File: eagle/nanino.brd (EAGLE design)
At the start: 68.6 x 53.3 mm, 19 parts, among them IC1 ATMEGA328P-20, Q1 16MHz

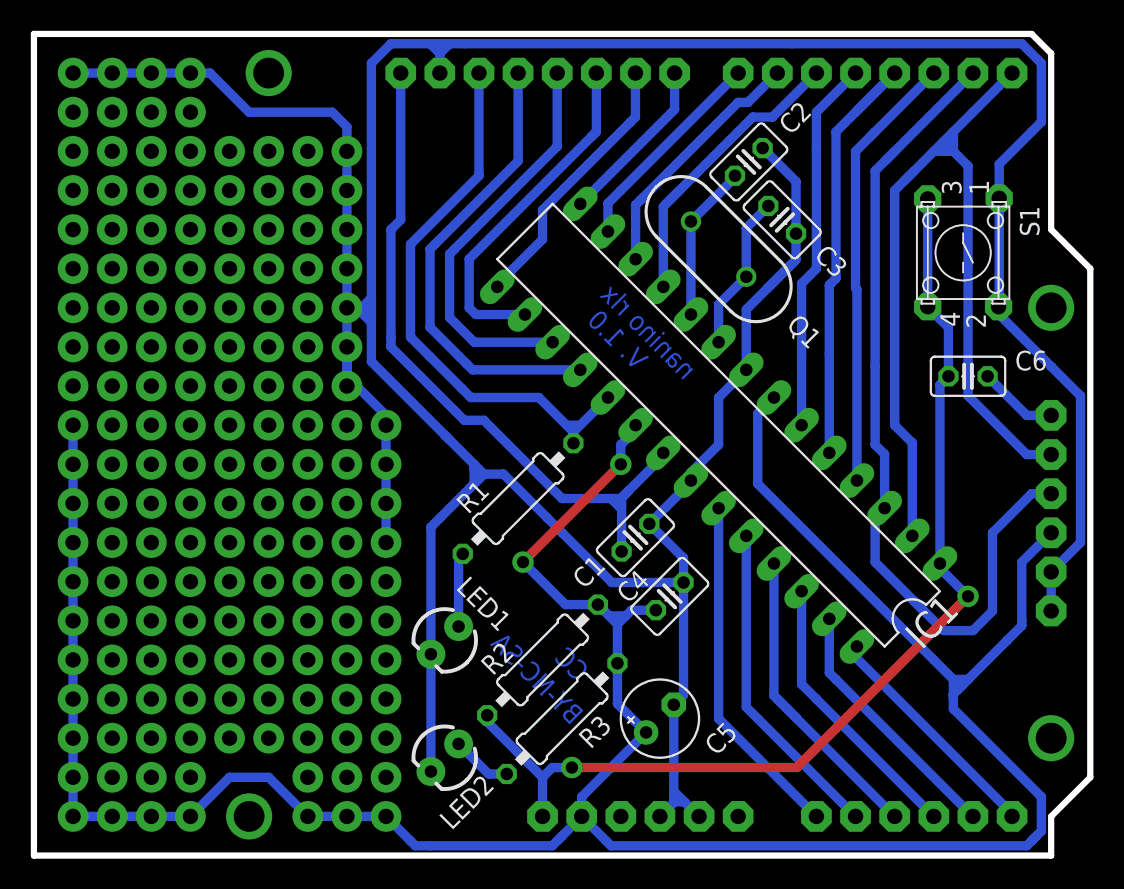
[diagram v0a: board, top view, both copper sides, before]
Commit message: improved routing
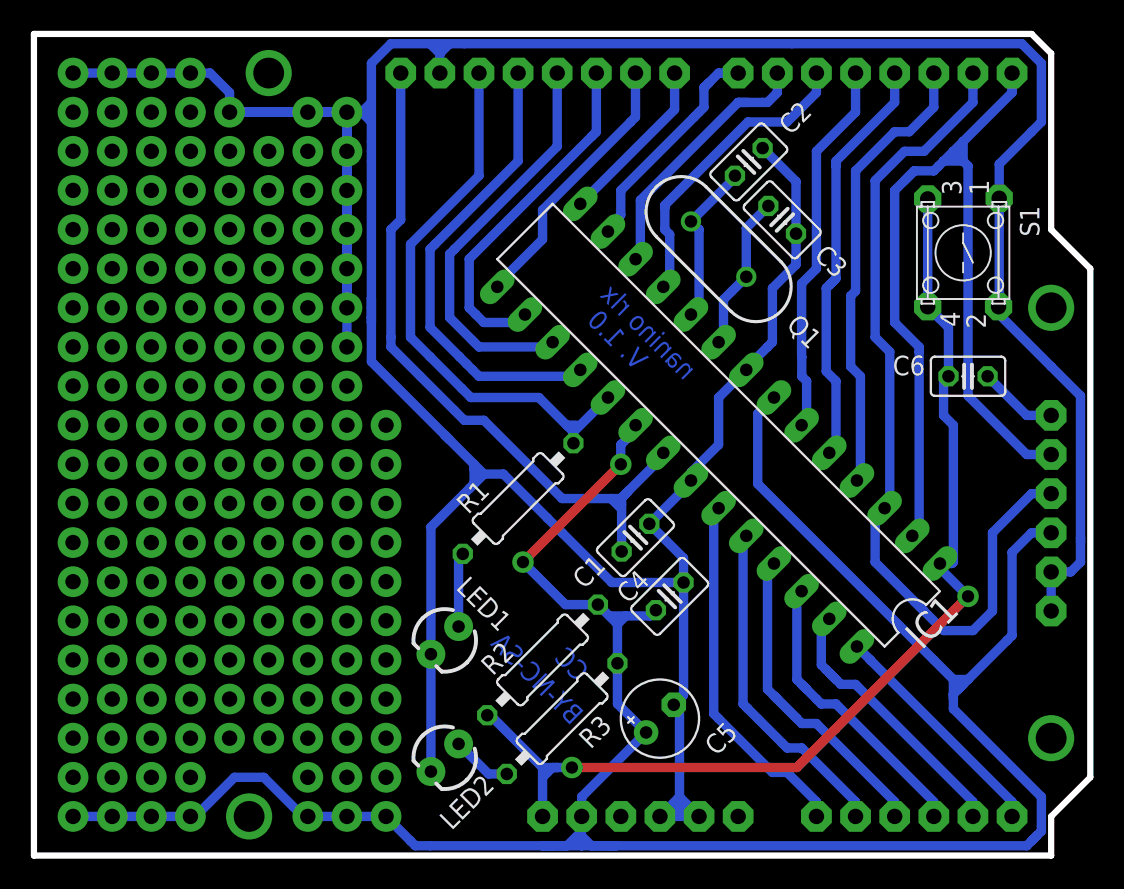
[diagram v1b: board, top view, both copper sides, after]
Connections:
- net GND renamed GND1
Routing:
- net VCC: track 183.8 -> 165.3 mm, vias 19 -> 9
- net N$39: track 0.00 -> 7.62 mm, vias 1 -> 3
- net GND1: track 269.1 -> 271.9 mm, vias 15 -> 10
- net N$24: track 69.0 -> 71.5 mm
- net N$4: track 30.0 -> 27.5 mm
- net N$21: track 16.7 -> 18.3 mm
- net N$7: track 16.3 -> 17.6 mm
- net N$19: track 21.8 -> 23.1 mm
- net N$20: track 18.2 -> 19.5 mm
- net N$8: track 13.8 -> 15.0 mm
- net N$1: track 62.5 -> 61.5 mm
- net N$18: track 21.2 -> 22.0 mm
- net N$17: track 22.6 -> 23.5 mm
- net N$3: track 29.0 -> 29.6 mm

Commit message: Version 1.1 - FTDI Rx/Tx corrected, bigger solder pads
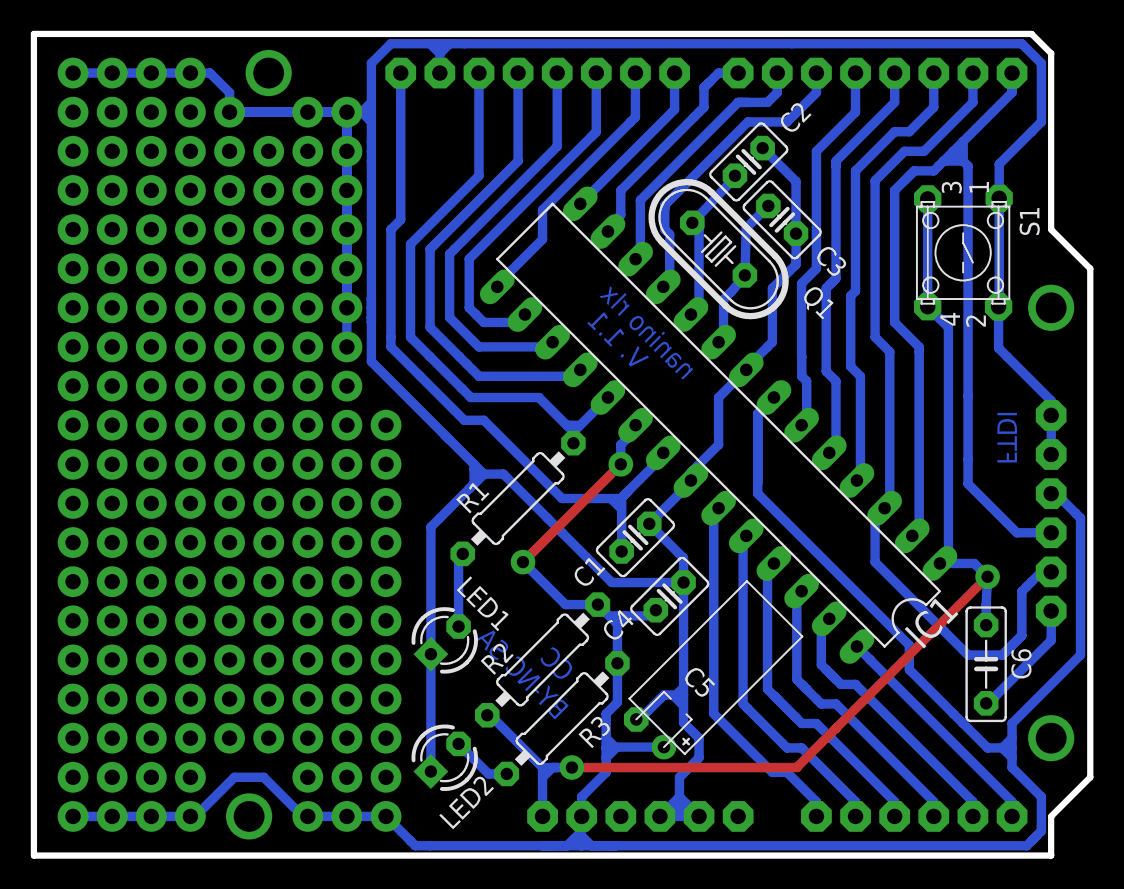
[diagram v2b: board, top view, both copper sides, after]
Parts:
- C1, C2, C3, C4: device rcl:C025-025X050 -> rc:C025-025X050
- C5: device elkos:E2,5-5 -> elkos:E2,5-5-L-12
- C6: device rcl:C025-025X050 -> rc:C050-025X075
- LED1, LED2: device SparkFun:LED3MM -> leds:LED3MM
- Q1: device SparkFun:HC49US -> crystals:HC49U-V
- R1, R2, R3: device rcl:0207/10 -> rc:0207/10
- moved C6 18.7 mm to (61.8, 12.4), turned to 90 degrees
- moved FTDI_ 2.54 mm to (67.3, 22.2), turned to 270 degrees
- moved C5 1.14 mm to (40.0, 7.94), turned to 135 degrees
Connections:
- net GND1 renamed GND
- net N$1: now also FTDI_.4; no longer FTDI_.5
- net N$2: now also FTDI_.5; no longer FTDI_.4
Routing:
- net VCC: track 165.3 -> 180.1 mm
- net GND: track 271.9 -> 263.3 mm
- net N$1: track 61.5 -> 66.9 mm
- net N$24: track 71.5 -> 76.0 mm
- net N$112: track 0.00 -> 3.83 mm
- net N$33: track 5.18 -> 7.82 mm
- net N$2: track 57.2 -> 56.0 mm
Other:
- board text added: "FTDI"
- board text added: "V. 1.1"
- board text removed: "V. 1.0"

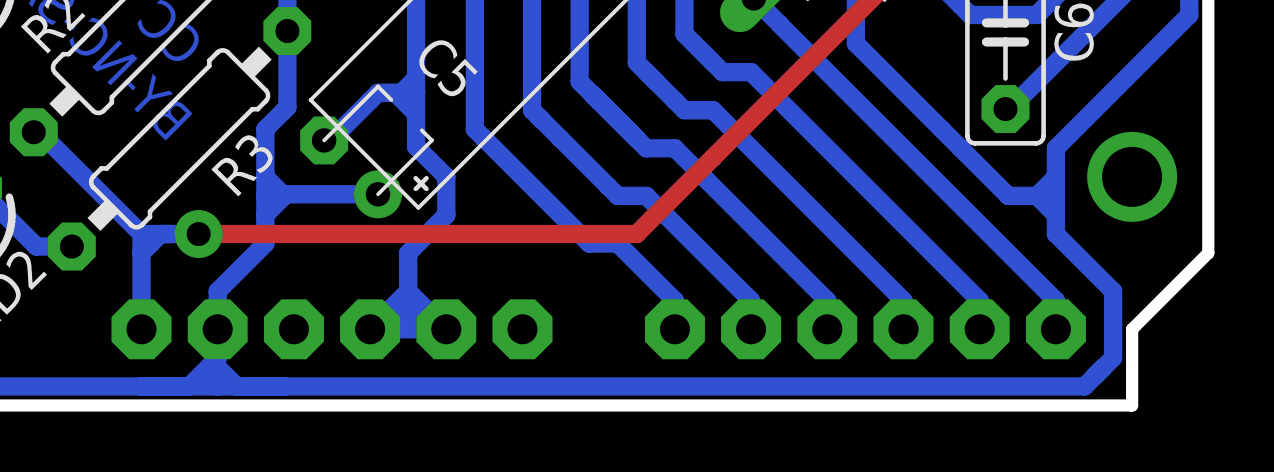
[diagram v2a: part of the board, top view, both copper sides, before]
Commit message: 5V power was connected to 3.3V Pin
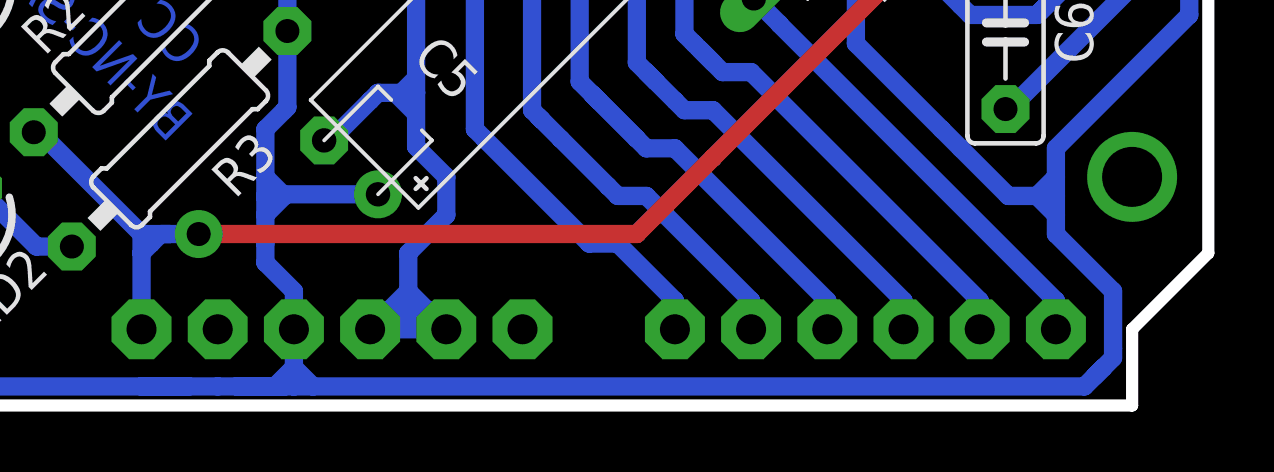
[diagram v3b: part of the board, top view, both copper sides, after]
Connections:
- net VCC: now also PWR_.3; no longer PWR_.2
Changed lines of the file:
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@@
 <layers>
 <layer number="1" name="Top" color="4" fill="1" visible="yes" active="yes"/>
-<layer number="16" name="Bottom" color="1" fill="1" visible="no" active="yes"/>
+<layer number="16" name="Bottom" color="1" fill="1" visible="yes" active="yes"/>
 <layer number="17" name="Pads" color="2" fill="1" visible="yes" active="yes"/>
 <layer number="18" name="Vias" color="2" fill="1" visible="yes" active="yes"/>
@@
 <contactref element="R2" pad="2"/>
 <contactref element="FTDI_" pad="3"/>
-<contactref element="PWR_" pad="2"/>
+<contactref element="PWR_" pad="3"/>
 <contactref element="IC1" pad="7"/>
 <contactref element="IC1" pad="20"/>
@@
 <wire x1="33.02" y1="0.635" x2="25.7175" y2="0.635" width="0.6096" layer="16"/>
 <wire x1="37.465" y1="0.635" x2="37.7825" y2="0.635" width="0.6096" layer="16"/>
-<wire x1="37.7825" y1="0.635" x2="64.4525" y2="0.635" width="0.6096" layer="16"/>
+<wire x1="37.7825" y1="0.635" x2="38.1" y2="0.635" width="0.6096" layer="16"/>
+<wire x1="38.1" y1="0.635" x2="38.735" y2="0.635" width="0.6096" layer="16"/>
+<wire x1="38.735" y1="0.635" x2="64.4525" y2="0.635" width="0.6096" layer="16"/>
 <wire x1="64.4525" y1="0.635" x2="65.0875" y2="1.27" width="0.6096" layer="16"/>
 <wire x1="24.4475" y1="0.9525" x2="24.765" y2="0.635" width="0.6096" layer="16"/>
 <wire x1="24.765" y1="0.635" x2="25.7175" y2="0.635" width="0.6096" layer="16"/>
-<wire x1="35.56" y1="2.54" x2="35.56" y2="1.5875" width="0.6096" layer="16"/>
-<wire x1="35.56" y1="1.5875" x2="34.6075" y2="0.635" width="0.6096" layer="16"/>
 <wire x1="34.6075" y1="0.635" x2="33.02" y2="0.635" width="0.6096" layer="16"/>
 <wire x1="33.02" y1="0.635" x2="35.56" y2="0.635" width="0.6096" layer="16"/>
 <wire x1="35.56" y1="0.635" x2="36.195" y2="0.635" width="0.6096" layer="16"/>
-<wire x1="36.195" y1="0.635" x2="37.7825" y2="0.635" width="0.6096" layer="16"/>
-<wire x1="37.7825" y1="0.635" x2="36.195" y2="0.635" width="0.6096" layer="16"/>
-<wire x1="36.195" y1="0.635" x2="35.56" y2="1.27" width="0.6096" layer="16"/>
-<wire x1="35.56" y1="1.27" x2="35.56" y2="0.635" width="0.6096" layer="16"/>
+<wire x1="36.195" y1="0.635" x2="37.465" y2="0.635" width="0.6096" layer="16"/>
+<wire x1="37.465" y1="0.635" x2="37.7825" y2="0.635" width="0.6096" layer="16"/>
+<wire x1="37.7825" y1="0.635" x2="37.465" y2="0.635" width="0.6096" layer="16"/>
+<wire x1="37.465" y1="0.635" x2="36.195" y2="0.635" width="0.6096" layer="16"/>
 <wire x1="38.4175" y1="15.5575" x2="40.005" y2="15.5575" width="0.6096" layer="16"/>
 <wire x1="40.005" y1="15.5575" x2="40.376971875" y2="15.929471875" width="0.6096" layer="16"/>
@@
 <wire x1="37.1475" y1="7.62" x2="37.1475" y2="6.985" width="0.6096" layer="16"/>
 <wire x1="37.1475" y1="6.985" x2="37.1475" y2="6.933471875" width="0.6096" layer="16"/>
-<wire x1="35.56" y1="2.54" x2="35.56" y2="3.81" width="0.6096" layer="16"/>
-<wire x1="35.56" y1="3.81" x2="37.1475" y2="5.3975" width="0.6096" layer="16"/>
 <wire x1="37.1475" y1="5.3975" x2="37.1475" y2="6.35" width="0.6096" layer="16"/>
 <wire x1="37.1475" y1="6.35" x2="37.1475" y2="6.933471875" width="0.6096" layer="16"/>
@@
 <wire x1="63.5" y1="7.62" x2="62.865" y2="6.985" width="0.6096" layer="16"/>
 <wire x1="62.865" y1="6.985" x2="63.5" y2="6.35" width="0.6096" layer="16"/>
+<wire x1="37.1475" y1="5.3975" x2="37.1475" y2="4.7625" width="0.6096" layer="16"/>
+<wire x1="37.1475" y1="4.7625" x2="38.1" y2="3.81" width="0.6096" layer="16"/>
+<wire x1="38.1" y1="3.81" x2="38.1" y2="2.54" width="0.6096" layer="16"/>
+<wire x1="38.1" y1="2.54" x2="38.1" y2="1.27" width="0.6096" layer="16"/>
+<wire x1="38.1" y1="1.27" x2="38.1" y2="0.635" width="0.6096" layer="16"/>
+<wire x1="38.1" y1="1.27" x2="38.735" y2="0.635" width="0.6096" layer="16"/>
+<wire x1="38.1" y1="1.27" x2="37.465" y2="0.635" width="0.6096" layer="16"/>
 </signal>
 <signal name="N$34">
@@
 </signal>
 </signals>
-<errors>
-</errors>
 </board>
 </drawing>
